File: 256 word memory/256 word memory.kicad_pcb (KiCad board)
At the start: 2 copper layers, 220 x 160 mm, 37 parts, among them J1 Conn_01x02_Male, J2 Conn_01x03_Male, J3 16-way-pcb-edge-Educ-8-connec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, J4 Conn_01x01_Male, J5 32-way-pcb-edge-Educ-8-connec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, U1 74LS05, U10 74LS95, U11 7400, U12 74LS00, U13 74LS93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

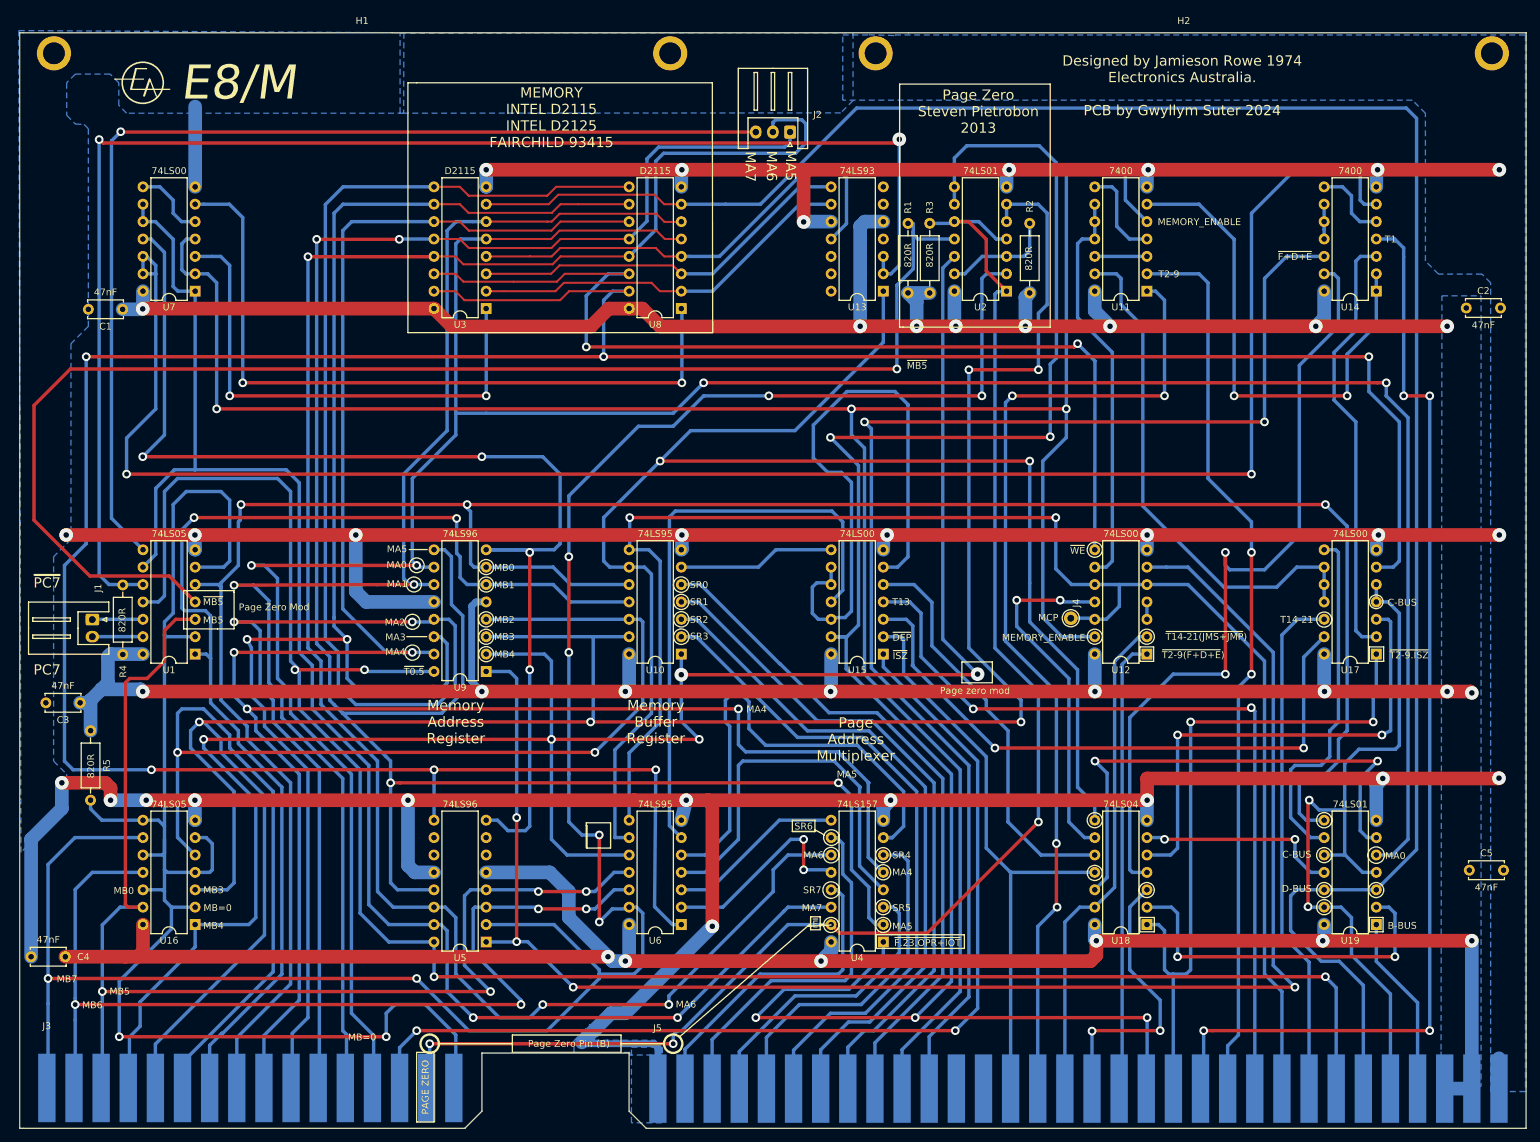
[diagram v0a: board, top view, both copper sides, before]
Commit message: Changes 20-7-2025 E8/T. Connected 3 missing supply rail tracks to ICS Added flood fill top and bottom to reduce noise E8/F Corrected labelling on RHS board to reflect EXT_LA not GND Changed fast slow switch operation so fast is in the DOWN position. E8/C. Ran a new track to the 2 pin JST connector from EXT_LA from 10 pin connector on SR input. Added files for E8MX, 2k byte memory expansion board
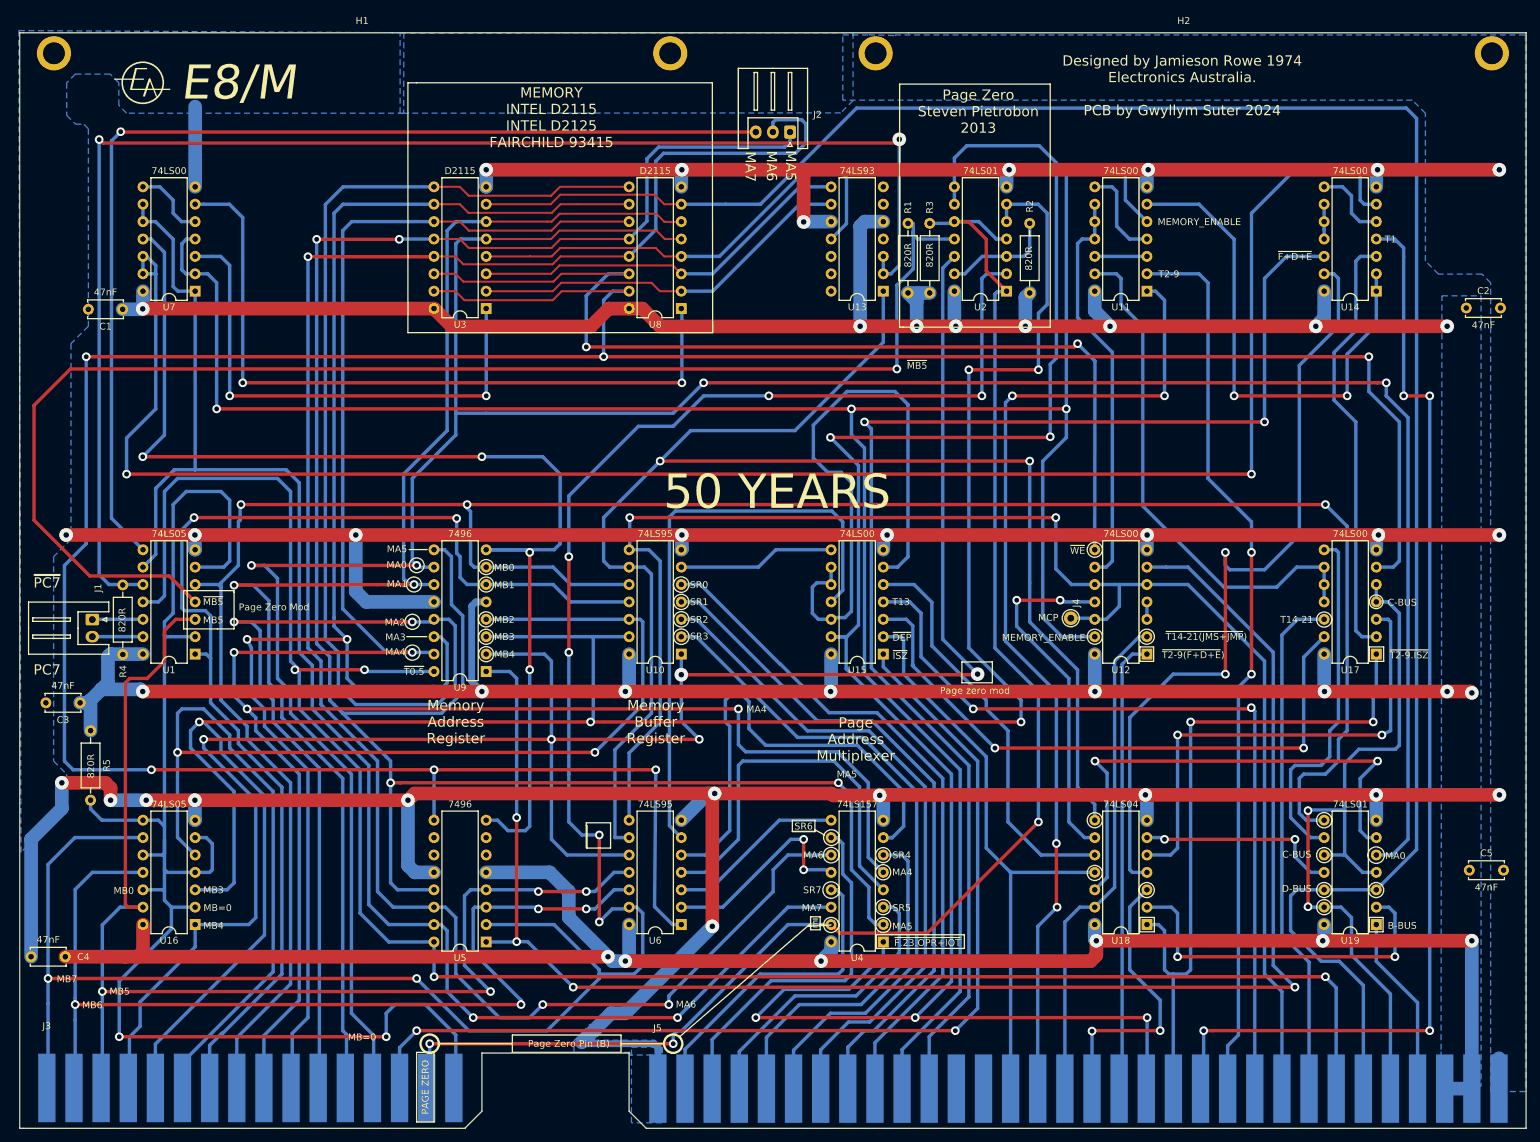
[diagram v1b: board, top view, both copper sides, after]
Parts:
- U11, U14: value 7400 -> 74LS00
- U5, U9: value 74LS96 -> 7496
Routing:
- net C-BUS: track 113.5 -> 111.5 mm
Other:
- board text added: "50 YEARS"
